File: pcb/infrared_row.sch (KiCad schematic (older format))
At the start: 16 parts, among them U2 QRE1113GR, U3 QRE1113GR, U4 QRE1113GR, U5 QRE1113GR, U6 QRE1113GR, U7 QRE1113GR, U8 QRE1113GR, U9 CD4051B

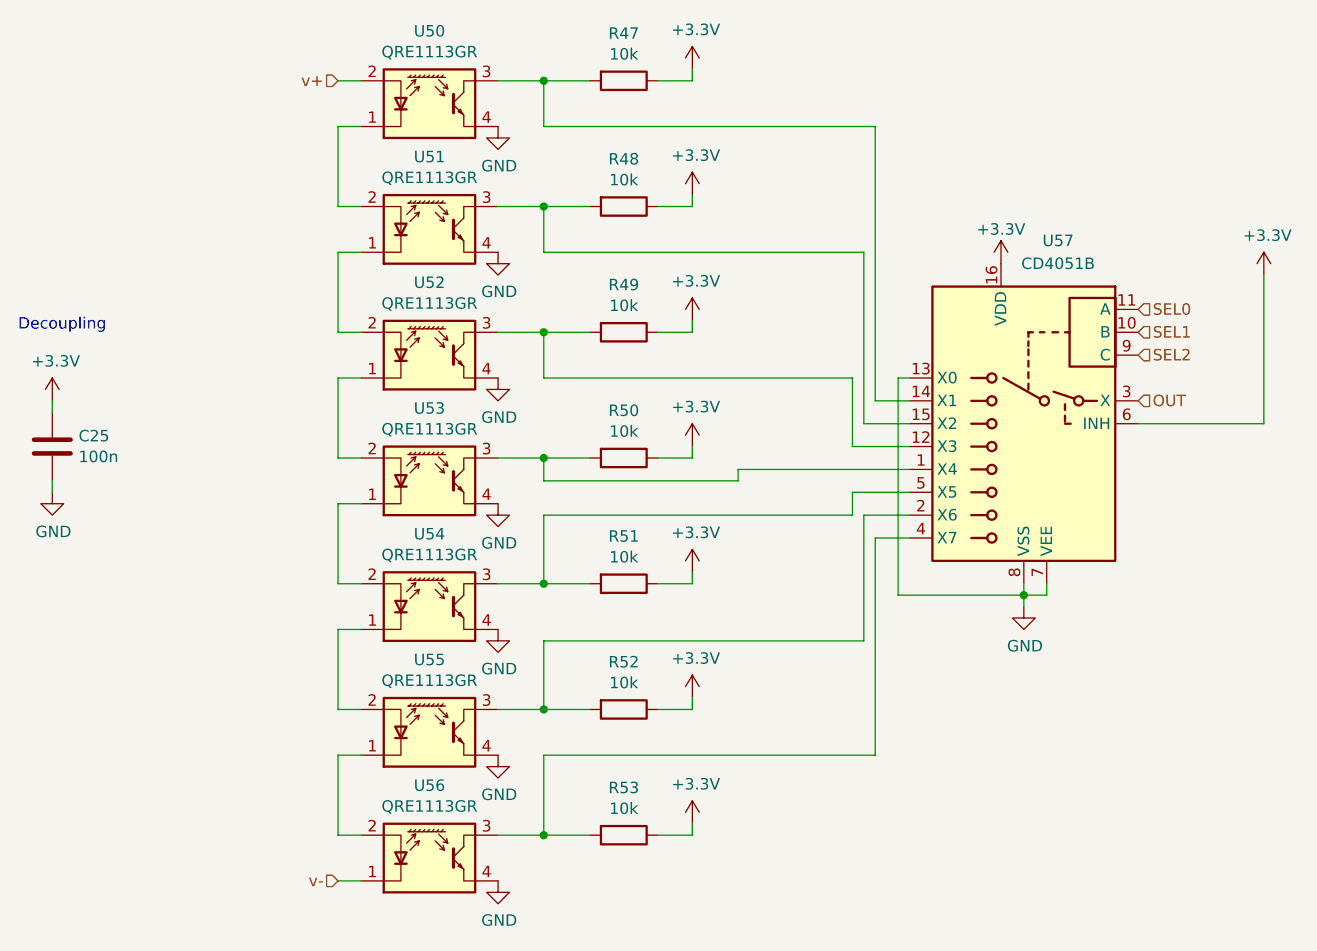
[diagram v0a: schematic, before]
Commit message: Connect IR Matrix to MCU
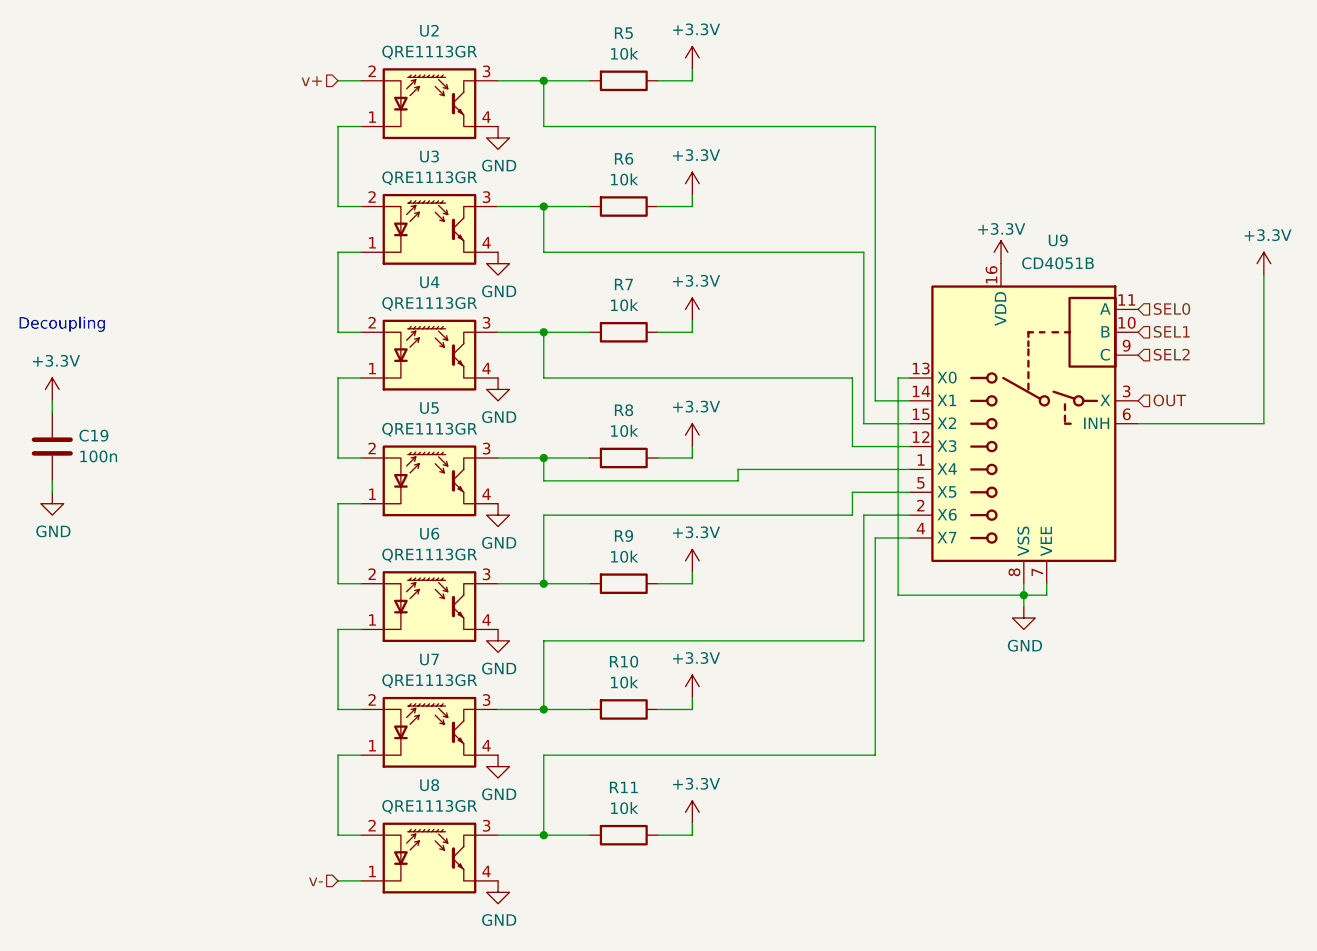
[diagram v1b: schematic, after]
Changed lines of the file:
@@
 $Descr A4 11693 8268
 encoding utf-8
-Sheet 7 12
+Sheet 5 12
 Title ""
 Date ""
@@
 AR Path="/5D1373A3/5D25183D/5D40DD62/5D29B58C" Ref="U41"  Part="1"
 AR Path="/5D1373A3/5D25183D/5D40E002/5D29B58C" Ref="U49"  Part="1"
-F 0 "U57" H 7950 4350 50  0000 C CNN
+F 0 "U9" H 7950 4350 50  0000 C CNN
 F 1 "CD4051B" H 7950 4250 50  0000 C CNN
 F 2 "Package_SO:SOP-16_4.55x10.3mm_P1.27mm" H 8250 2800 50  0001 L CNN
@@
 AR Path="/5D1373A3/5D25183D/5D40DD62/5D2F9ADC" Ref="C23"  Part="1"
 AR Path="/5D1373A3/5D25183D/5D40E002/5D2F9ADC" Ref="C24"  Part="1"
-F 0 "C25" H 3965 3696 50  0000 L CNN
+F 0 "C19" H 3965 3696 50  0000 L CNN
 F 1 "100n" H 3965 3605 50  0000 L CNN
 F 2 "Capacitor_SMD:C_0805_2012Metric" H 3888 3500 50  0001 C CNN
@@
 AR Path="/5D1373A3/5D25183D/5D40DD62/5D37CE94" Ref="U39"  Part="1"
 AR Path="/5D1373A3/5D25183D/5D40E002/5D37CE94" Ref="U47"  Part="1"
-F 0 "U55" H 5500 5217 50  0000 C CNN
+F 0 "U7" H 5500 5217 50  0000 C CNN
 F 1 "QRE1113GR" H 5500 5126 50  0000 C CNN
 F 2 "OptoDevice:OnSemi_CASE100CY" H 5500 4700 50  0001 C CNN
@@
 AR Path="/5D1373A3/5D25183D/5D40DD62/5D37CE9A" Ref="U38"  Part="1"
 AR Path="/5D1373A3/5D25183D/5D40E002/5D37CE9A" Ref="U46"  Part="1"
-F 0 "U54" H 5500 4667 50  0000 C CNN
+F 0 "U6" H 5500 4667 50  0000 C CNN
 F 1 "QRE1113GR" H 5500 4576 50  0000 C CNN
 F 2 "OptoDevice:OnSemi_CASE100CY" H 5500 4150 50  0001 C CNN
@@
 AR Path="/5D1373A3/5D25183D/5D40DD62/5D37CEA0" Ref="U37"  Part="1"
 AR Path="/5D1373A3/5D25183D/5D40E002/5D37CEA0" Ref="U45"  Part="1"
-F 0 "U53" H 5500 4117 50  0000 C CNN
+F 0 "U5" H 5500 4117 50  0000 C CNN
 F 1 "QRE1113GR" H 5500 4026 50  0000 C CNN
 F 2 "OptoDevice:OnSemi_CASE100CY" H 5500 3600 50  0001 C CNN
@@
 AR Path="/5D1373A3/5D25183D/5D40DD62/5D37CEA6" Ref="U36"  Part="1"
 AR Path="/5D1373A3/5D25183D/5D40E002/5D37CEA6" Ref="U44"  Part="1"
-F 0 "U52" H 5500 3567 50  0000 C CNN
+F 0 "U4" H 5500 3567 50  0000 C CNN
 F 1 "QRE1113GR" H 5500 3476 50  0000 C CNN
 F 2 "OptoDevice:OnSemi_CASE100CY" H 5500 3050 50  0001 C CNN
@@
 AR Path="/5D1373A3/5D25183D/5D40DD62/5D37CEB8" Ref="U35"  Part="1"
 AR Path="/5D1373A3/5D25183D/5D40E002/5D37CEB8" Ref="U43"  Part="1"
-F 0 "U51" H 5500 3017 50  0000 C CNN
+F 0 "U3" H 5500 3017 50  0000 C CNN
 F 1 "QRE1113GR" H 5500 2926 50  0000 C CNN
 F 2 "OptoDevice:OnSemi_CASE100CY" H 5500 2500 50  0001 C CNN
@@
 AR Path="/5D1373A3/5D25183D/5D40DD62/5D37CED0" Ref="U34"  Part="1"
 AR Path="/5D1373A3/5D25183D/5D40E002/5D37CED0" Ref="U42"  Part="1"
-F 0 "U50" H 5500 2467 50  0000 C CNN
+F 0 "U2" H 5500 2467 50  0000 C CNN
 F 1 "QRE1113GR" H 5500 2376 50  0000 C CNN
 F 2 "OptoDevice:OnSemi_CASE100CY" H 5500 1950 50  0001 C CNN
@@
 AR Path="/5D1373A3/5D25183D/5D40DD62/5D37CED6" Ref="R33"  Part="1"
 AR Path="/5D1373A3/5D25183D/5D40E002/5D37CED6" Ref="R40"  Part="1"
-F 0 "R47" V 6143 2050 50  0000 C CNN
+F 0 "R5" V 6143 2050 50  0000 C CNN
 F 1 "10k" V 6234 2050 50  0000 C CNN
 F 2 "Resistor_SMD:R_0805_2012Metric" V 6280 2050 50  0001 C CNN
@@
 AR Path="/5D1373A3/5D25183D/5D40DD62/5D37CEE4" Ref="R34"  Part="1"
 AR Path="/5D1373A3/5D25183D/5D40E002/5D37CEE4" Ref="R41"  Part="1"
-F 0 "R48" V 6143 2600 50  0000 C CNN
+F 0 "R6" V 6143 2600 50  0000 C CNN
 F 1 "10k" V 6234 2600 50  0000 C CNN
 F 2 "Resistor_SMD:R_0805_2012Metric" V 6280 2600 50  0001 C CNN
@@
 AR Path="/5D1373A3/5D25183D/5D40DD62/5D37CEF2" Ref="R35"  Part="1"
 AR Path="/5D1373A3/5D25183D/5D40E002/5D37CEF2" Ref="R42"  Part="1"
-F 0 "R49" V 6143 3150 50  0000 C CNN
+F 0 "R7" V 6143 3150 50  0000 C CNN
 F 1 "10k" V 6234 3150 50  0000 C CNN
 F 2 "Resistor_SMD:R_0805_2012Metric" V 6280 3150 50  0001 C CNN
@@
 AR Path="/5D1373A3/5D25183D/5D40DD62/5D37CF00" Ref="R36"  Part="1"
 AR Path="/5D1373A3/5D25183D/5D40E002/5D37CF00" Ref="R43"  Part="1"
-F 0 "R50" V 6143 3700 50  0000 C CNN
+F 0 "R8" V 6143 3700 50  0000 C CNN
 F 1 "10k" V 6234 3700 50  0000 C CNN
 F 2 "Resistor_SMD:R_0805_2012Metric" V 6280 3700 50  0001 C CNN
@@
 AR Path="/5D1373A3/5D25183D/5D40DD62/5D37CF0E" Ref="R37"  Part="1"
 AR Path="/5D1373A3/5D25183D/5D40E002/5D37CF0E" Ref="R44"  Part="1"
-F 0 "R51" V 6143 4250 50  0000 C CNN
+F 0 "R9" V 6143 4250 50  0000 C CNN
 F 1 "10k" V 6234 4250 50  0000 C CNN
 F 2 "Resistor_SMD:R_0805_2012Metric" V 6280 4250 50  0001 C CNN
@@
 AR Path="/5D1373A3/5D25183D/5D40DD62/5D37CF1C" Ref="R38"  Part="1"
 AR Path="/5D1373A3/5D25183D/5D40E002/5D37CF1C" Ref="R45"  Part="1"
-F 0 "R52" V 6143 4800 50  0000 C CNN
+F 0 "R10" V 6143 4800 50  0000 C CNN
 F 1 "10k" V 6234 4800 50  0000 C CNN
 F 2 "Resistor_SMD:R_0805_2012Metric" V 6280 4800 50  0001 C CNN
@@
 AR Path="/5D1373A3/5D25183D/5D40DD62/5D37CF2A" Ref="R39"  Part="1"
 AR Path="/5D1373A3/5D25183D/5D40E002/5D37CF2A" Ref="R46"  Part="1"
-F 0 "R53" V 6143 5350 50  0000 C CNN
+F 0 "R11" V 6143 5350 50  0000 C CNN
 F 1 "10k" V 6234 5350 50  0000 C CNN
 F 2 "Resistor_SMD:R_0805_2012Metric" V 6280 5350 50  0001 C CNN
@@
 AR Path="/5D1373A3/5D25183D/5D40DD62/5D37CF65" Ref="U40"  Part="1"
 AR Path="/5D1373A3/5D25183D/5D40E002/5D37CF65" Ref="U48"  Part="1"
-F 0 "U56" H 5500 5767 50  0000 C CNN
+F 0 "U8" H 5500 5767 50  0000 C CNN
 F 1 "QRE1113GR" H 5500 5676 50  0000 C CNN
 F 2 "OptoDevice:OnSemi_CASE100CY" H 5500 5250 50  0001 C CNN
